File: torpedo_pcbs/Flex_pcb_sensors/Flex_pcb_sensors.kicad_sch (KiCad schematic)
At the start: 2 parts, among them J1 Conn_01x08, U1 MS583702BA01-50

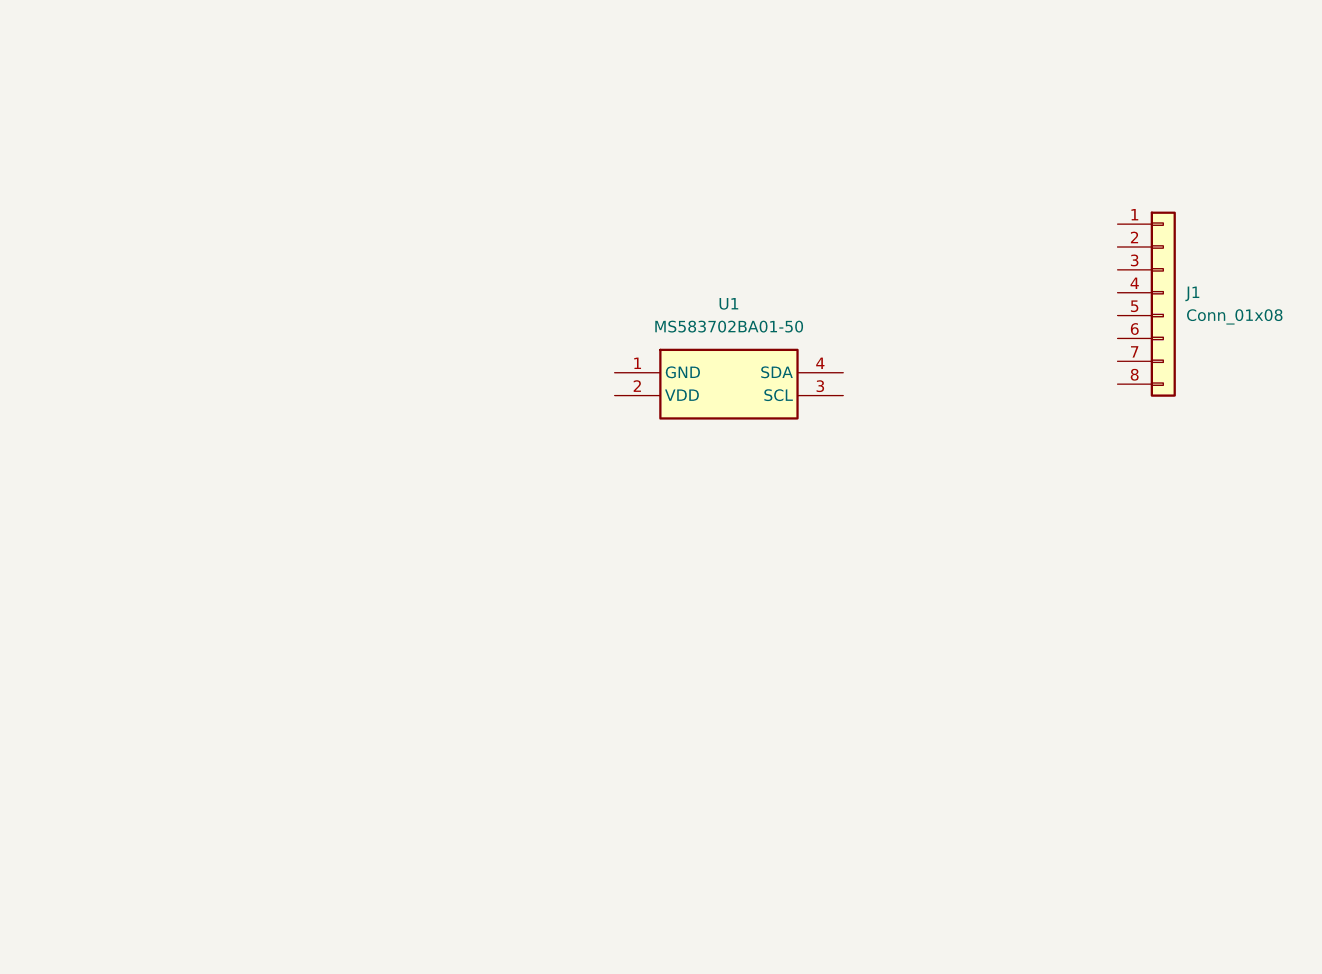
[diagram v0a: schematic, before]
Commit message: sensors pcb and main pcb improvements
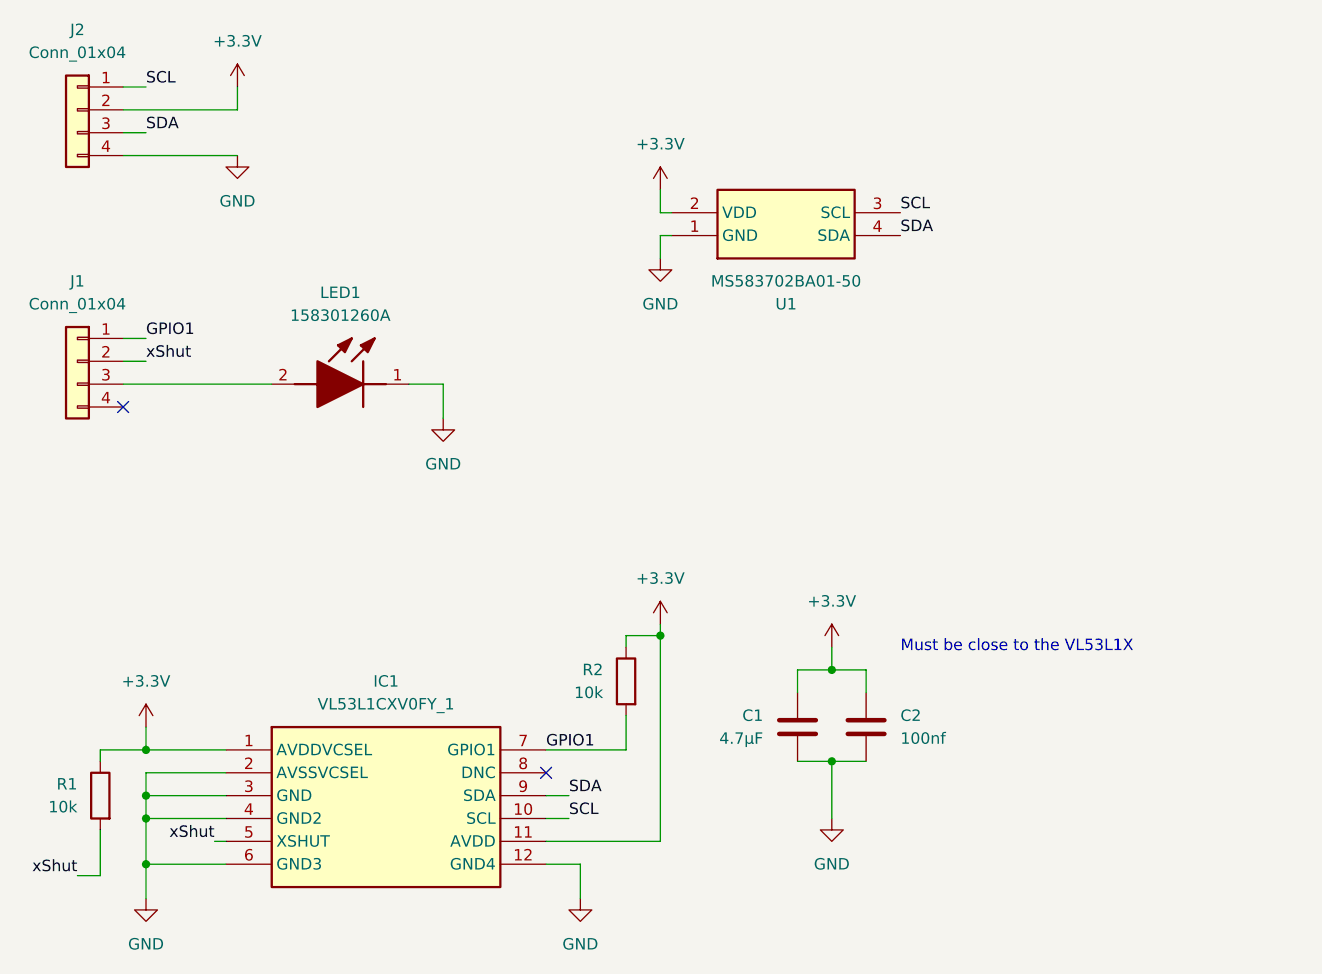
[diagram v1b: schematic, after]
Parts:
- removed J1: Conn_01x08, symbol Connector_Generic:Conn_01x08
- added C1: 4.7μF, Capacitor_SMD:C_0603_1608Metric, symbol Device:C
- added C2: 100nf, Capacitor_SMD:C_0603_1608Metric, symbol Device:C
- added IC1: VL53L1CXV0FY_1, SamacSys_Parts:VL53L1CXV0FY1, symbol SamacSys_Parts:VL53L1CXV0FY_1
- added J1, J2: Conn_01x04, fpc fcc conn:4pos fpc conn, symbol Connector_Generic:Conn_01x04
- added LED1: 158301260A, 158301260A, symbol SamacSys_Parts:158301260A
- added R1, R2: 10k, Resistor_SMD:R_0603_1608Metric, symbol Device:R
- U1: footprint MS583702BA0150 -> SamacSys_Parts:MS583702BA0150
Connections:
- net GND: now reaches U1.1 (GND)
- net GND: now also C1.2, C2.2, IC1.12 (GND4), IC1.2 (AVSSVCSEL), IC1.3 (GND), IC1.4 (GND2), IC1.6 (GND3), J2.4 (Pin_4), LED1.1 (K)
- net +3.3V: now reaches U1.2 (VDD)
- net +3.3V: now also C1.1, C2.1, IC1.1 (AVDDVCSEL), IC1.11 (AVDD), J2.2 (Pin_2), R1.1, R2.1
- net SCL: now reaches U1.3 (SCL)
- net SCL: now also IC1.10 (SCL), J2.1 (Pin_1)
- net SDA: now reaches U1.4 (SDA)
- net SDA: now also IC1.9 (SDA), J2.3 (Pin_3)
- new net: J1.3 (Pin_3), LED1.2 (A)
- new net GPIO1: IC1.7 (GPIO1), J1.1 (Pin_1), R2.2
- new net xShut: IC1.5 (XSHUT), J1.2 (Pin_2), R1.2
- no-connect marks 0 -> 2
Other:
- note added: "Must be close to the VL53L1X"
- moved on the sheet: U1

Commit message: flex_pcb_updates
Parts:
- added J3: mounting, MountingEquipment:small mounting holes, symbol Connector_Generic:Conn_01x02
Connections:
- net GND: now also J3.1 (Pin_1), J3.2 (Pin_2)
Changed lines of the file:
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@@
 	(paper "A4")
+	(junction
+		(at 92.71 63.5)
+		(diameter 0)
+		(color 0 0 0 0)
+	)
 	(junction
 		(at 29.21 102.87)
@@
 	(wire
 		(pts
+			(xy 92.71 63.5) (xy 92.71 66.04)
+		)
+		(stroke
+			(width 0)
+			(type default)
+		)
+	)
+	(wire
+		(pts
 			(xy 77.47 110.49) (xy 73.66 110.49)
 		)
@@
 		(pts
 			(xy 86.36 83.82) (xy 86.36 85.09)
+		)
+		(stroke
+			(width 0)
+			(type default)
+		)
+	)
+	(wire
+		(pts
+			(xy 92.71 60.96) (xy 92.71 63.5)
 		)
 		(stroke
@@
 				(path "/e481a0a7-d92f-423b-8454-fe10047fa3c9"
 					(reference "#PWR06")
+					(unit 1)
+				)
+			)
+		)
+	)
+	(symbol
+		(lib_id "Connector_Generic:Conn_01x02")
+		(at 87.63 60.96 0)
+		(mirror y)
+		(unit 1)
+		(exclude_from_sim no)
+		(in_bom yes)
+		(on_board yes)
+		(dnp no)
+		(fields_autoplaced yes)
+		(property "Reference" "J3"
+			(at 87.63 54.61 0)
+			(effects
+				(font
+					(size 1.27 1.27)
+				)
+			)
+		)
+		(property "Value" "mounting"
+			(at 87.63 57.15 0)
+			(effects
+				(font
+					(size 1.27 1.27)
+				)
+			)
+		)
+		(property "Footprint" "MountingEquipment:small mounting holes"
+			(at 87.63 60.96 0)
+			(effects
+				(font
+					(size 1.27 1.27)
+				)
+				(hide yes)
+			)
+		)
+		(property "Datasheet" "~"
+			(at 87.63 60.96 0)
+			(effects
+				(font
+					(size 1.27 1.27)
+				)
+				(hide yes)
+			)
+		)
+		(property "Description" "Generic connector, single row, 01x02, script generated (kicad-library-utils/schlib/autogen/connector/)"
+			(at 87.63 60.96 0)
+			(effects
+				(font
+					(size 1.27 1.27)
+				)
+				(hide yes)
+			)
+		)
+		(pin "2"
+		)
+		(pin "1"
+		)
+		(instances
+			(project "Flex_pcb_sensors"
+				(path "/e481a0a7-d92f-423b-8454-fe10047fa3c9"
+					(reference "J3")
 					(unit 1)
 				)
@@
 					(unit 1)
 				)
+			)
+		)
+	)
+	(symbol
+		(lib_id "power:GND")
+		(at 92.71 66.04 0)
+		(unit 1)
+		(exclude_from_sim no)
+		(in_bom yes)
+		(on_board yes)
+		(dnp no)
+		(fields_autoplaced yes)
+		(property "Reference" "#PWR012"
+			(at 92.71 72.39 0)
+			(effects
+				(font
+					(size 1.27 1.27)
+				)
+				(hide yes)
+			)
+		)
+		(property "Value" "GND"
+			(at 92.71 71.12 0)
+			(effects
+				(font
+					(size 1.27 1.27)
+				)
+			)
+		)
+		(property "Footprint" ""
+			(at 92.71 66.04 0)
+			(effects
+				(font
+					(size 1.27 1.27)
+				)
+				(hide yes)
+			)
+		)
+		(property "Datasheet" ""
+			(at 92.71 66.04 0)
+			(effects
+				(font
+					(size 1.27 1.27)
+				)
+				(hide yes)
+			)
+		)
+		(property "Description" "Power symbol creates a global label with name \"GND\" , ground"
+			(at 92.71 66.04 0)
+			(effects
+				(font
+					(size 1.27 1.27)
+				)
+				(hide yes)
+			)
+		)
+		(pin "1"
+		)
+		(instances
+			(project "Flex_pcb_sensors"
+				(path "/e481a0a7-d92f-423b-8454-fe10047fa3c9"
+					(reference "#PWR012")
+					(unit 1)
+				)

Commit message: everything is connected
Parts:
- removed J3: mounting, MountingEquipment:small mounting holes, symbol Connector_Generic:Conn_01x02
- removed LED1: 158301260A, 158301260A, symbol SamacSys_Parts:158301260A
- added C3: 100nf, Capacitor_SMD:C_0603_1608Metric, symbol Device:C
- U1: LCSC (none) -> C5785272
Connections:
- net +3.3V: now also C3.1
- net GND: now also C3.2
- no-connect marks 2 -> 4

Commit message: June-1-2025 jlcpcb order
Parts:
- added J3, J8: Conn_01x01, TestPoint:TestPoint_Pad_1.0x1.0mm, symbol Connector_Generic:Conn_01x01
- C1: LCSC (none) -> C1705
- C2, C3: LCSC (none) -> C24452
- IC1: LCSC (none) -> C190004
- R1, R2: LCSC (none) -> C25804
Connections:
- net +3.3V: now also J1.1 (Pin_1), J2.3 (Pin_3); no longer J2.2 (Pin_2)
- net GND: now also J1.2 (Pin_2)
- net GPIO1: now also J1.3 (Pin_3); no longer J1.1 (Pin_1)
- net SCL: now also J8.1 (Pin_1)
- net SDA: now also J2.2 (Pin_2), J3.1 (Pin_1); no longer J2.3 (Pin_3)
- net xShut: now also J1.4 (Pin_4); no longer J1.2 (Pin_2)
- no-connect marks 4 -> 1
